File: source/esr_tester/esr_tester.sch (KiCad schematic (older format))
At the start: 40 parts, among them IC1-1 TL084, J1 Conn_01x01, J2 Conn_01x01

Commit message: Import netlist into Pcbnew.
Arrange footprints as in the magazine article.

Draw a board edge.
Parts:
- BT1: footprint Pin_Headers:Pin_Header_Straight_1x02_Pitch2.54mm -> Socket_Strips:Socket_Strip_Straight_1x01_Pitch2.54mm
- C3, C4: footprint Capacitors_THT:C_Disc_D3.0mm_W1.6mm_P2.50mm -> Capacitors_THT:C_Rect_L7.0mm_W2.5mm_P5.00mm
- C5, C6: footprint Capacitors_THT:C_Disc_D3.0mm_W1.6mm_P2.50mm -> Capacitors_THT:C_Rect_L7.0mm_W4.5mm_P5.00mm
- DS1, DS2, DS3: footprint Diodes_THT:D_5W_P5.08mm_Vertical_AnodeUp -> Diodes_THT:D_DO-35_SOD27_P7.62mm_Horizontal
- R1, R10, R11, R12, R13, R14, R15, R16, R17, R18, R19, R2, R20, R3, R4, R5, R6, R7, R8, R9: footprint Resistors_THT:R_Axial_DIN0204_L3.6mm_D1.6mm_P5.08mm_Horizontal -> Resistors_THT:R_Axial_DIN0204_L3.6mm_D1.6mm_P7.62mm_Horizontal
- R21: footprint Potentiometers:Potentiometer_Trimmer_ACP_CA9v_Horizontal_Px10.0mm_Py5.0mm -> Potentiometers:Potentiometer_Trimmer_Bourns_3266Y
- S1: footprint Buttons_Switches_THT:SW_PUSH-12mm -> Socket_Strips:Socket_Strip_Straight_1x03_Pitch2.54mm
- TR1, TR2, TR3: footprint TO_SOT_Packages_THT:TO-92_Molded_Narrow -> TO_SOT_Packages_THT:TO-92_Inline_Wide

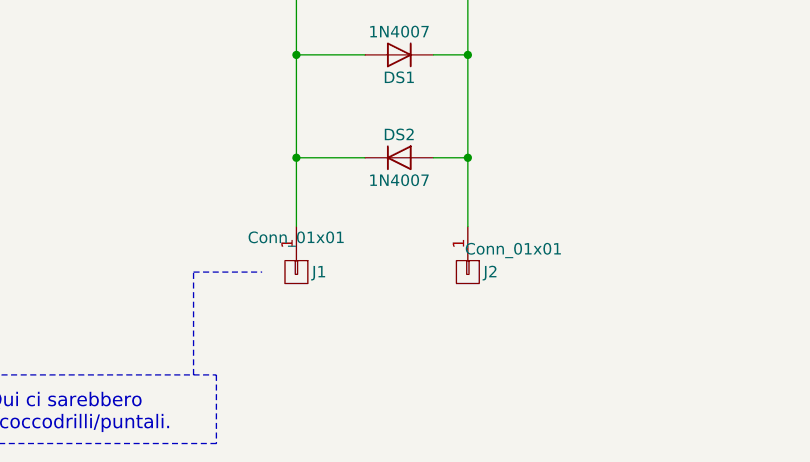
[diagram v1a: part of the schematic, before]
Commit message: The branch proto2 is for a prototype build with stripboard.
Schematics: changed connector for testing probes (one connector with
two poles instead of two with one each).

CvPcb: Changed some connectors, resistors and diodes footprints.

Pcbnew: A new layout for a stripboard.
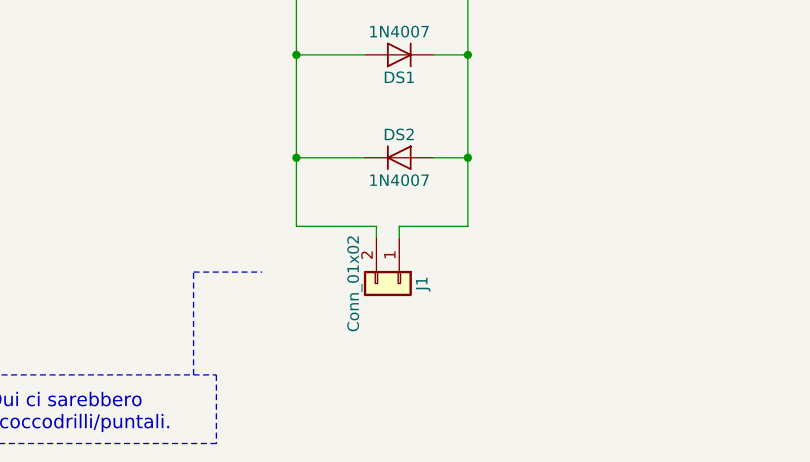
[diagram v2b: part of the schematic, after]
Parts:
- removed J1, J2: Conn_01x01, Connectors:Banana_Jack_1Pin, symbol CONN_01X01
- added J1: Conn_01x02, Socket_Strips:Socket_Strip_Straight_1x02_Pitch2.54mm, symbol Conn_01x02
- BT1: footprint Socket_Strips:Socket_Strip_Straight_1x01_Pitch2.54mm -> Socket_Strips:Socket_Strip_Straight_1x02_Pitch2.54mm
- DS1, DS2, DS3: footprint Diodes_THT:D_DO-35_SOD27_P7.62mm_Horizontal -> Diodes_THT:D_DO-35_SOD27_P2.54mm_Vertical_KathodeUp
- MES1: footprint Connectors:Banana_Jack_2Pin -> Socket_Strips:Socket_Strip_Straight_1x02_Pitch2.54mm
- R1, R10, R11, R12, R13, R14, R15, R16, R17, R18, R19, R2, R20, R3, R4, R5, R6, R7, R8, R9: footprint Resistors_THT:R_Axial_DIN0204_L3.6mm_D1.6mm_P7.62mm_Horizontal -> Resistors_THT:R_Axial_DIN0207_L6.3mm_D2.5mm_P2.54mm_Vertical
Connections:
- net GND: now also J1.1 (Pin_1)
- net at DS1.2 (A), DS2.1 (K), R10.2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: now also J1.2 (Pin_2)
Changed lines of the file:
@@
 F 0 "R4" V 2980 1300 50  0000 C CNN
 F 1 "10k" V 2900 1300 50  0000 C CNN
-F 2 "Resistors_THT:R_Axial_DIN0204_L3.6mm_D1.6mm_P7.62mm_Horizontal" V 2830 1300 50  0001 C CNN
+F 2 "Resistors_THT:R_Axial_DIN0207_L6.3mm_D2.5mm_P2.54mm_Vertical" V 2830 1300 50  0001 C CNN
 F 3 "" H 2900 1300 50  0001 C CNN
 	1    2900 1300
@@
 F 0 "R5" V 2980 2250 50  0000 C CNN
 F 1 "10k" V 2900 2250 50  0000 C CNN
-F 2 "Resistors_THT:R_Axial_DIN0204_L3.6mm_D1.6mm_P7.62mm_Horizontal" V 2830 2250 50  0001 C CNN
+F 2 "Resistors_THT:R_Axial_DIN0207_L6.3mm_D2.5mm_P2.54mm_Vertical" V 2830 2250 50  0001 C CNN
 F 3 "" H 2900 2250 50  0001 C CNN
 	1    2900 2250
@@
 F 0 "R1" V 1930 4600 50  0000 C CNN
 F 1 "1.5k" V 1850 4600 50  0000 C CNN
-F 2 "Resistors_THT:R_Axial_DIN0204_L3.6mm_D1.6mm_P7.62mm_Horizontal" V 1780 4600 50  0001 C CNN
+F 2 "Resistors_THT:R_Axial_DIN0207_L6.3mm_D2.5mm_P2.54mm_Vertical" V 1780 4600 50  0001 C CNN
 F 3 "" H 1850 4600 50  0001 C CNN
 	1    1850 4600
@@
 F 0 "R2" V 2730 3350 50  0000 C CNN
 F 1 "10k" V 2650 3350 50  0000 C CNN
-F 2 "Resistors_THT:R_Axial_DIN0204_L3.6mm_D1.6mm_P7.62mm_Horizontal" V 2580 3350 50  0001 C CNN
+F 2 "Resistors_THT:R_Axial_DIN0207_L6.3mm_D2.5mm_P2.54mm_Vertical" V 2580 3350 50  0001 C CNN
 F 3 "" H 2650 3350 50  0001 C CNN
 	1    2650 3350
@@
 F 0 "R3" V 2780 4600 50  0000 C CNN
 F 1 "10k" V 2700 4600 50  0000 C CNN
-F 2 "Resistors_THT:R_Axial_DIN0204_L3.6mm_D1.6mm_P7.62mm_Horizontal" V 2630 4600 50  0001 C CNN
+F 2 "Resistors_THT:R_Axial_DIN0207_L6.3mm_D2.5mm_P2.54mm_Vertical" V 2630 4600 50  0001 C CNN
 F 3 "" H 2700 4600 50  0001 C CNN
 	1    2700 4600
@@
 F 0 "R6" V 3280 3950 50  0000 C CNN
 F 1 "68k" V 3200 3950 50  0000 C CNN
-F 2 "Resistors_THT:R_Axial_DIN0204_L3.6mm_D1.6mm_P7.62mm_Horizontal" V 3130 3950 50  0001 C CNN
+F 2 "Resistors_THT:R_Axial_DIN0207_L6.3mm_D2.5mm_P2.54mm_Vertical" V 3130 3950 50  0001 C CNN
 F 3 "" H 3200 3950 50  0001 C CNN
 	1    3200 3950
@@
 F 0 "R8" V 3980 3300 50  0000 C CNN
 F 1 "12k" V 3900 3300 50  0000 C CNN
-F 2 "Resistors_THT:R_Axial_DIN0204_L3.6mm_D1.6mm_P7.62mm_Horizontal" V 3830 3300 50  0001 C CNN
+F 2 "Resistors_THT:R_Axial_DIN0207_L6.3mm_D2.5mm_P2.54mm_Vertical" V 3830 3300 50  0001 C CNN
 F 3 "" H 3900 3300 50  0001 C CNN
 	1    3900 3300
@@
 F 0 "R7" V 3980 1400 50  0000 C CNN
 F 1 "4.7k" V 3900 1400 50  0000 C CNN
-F 2 "Resistors_THT:R_Axial_DIN0204_L3.6mm_D1.6mm_P7.62mm_Horizontal" V 3830 1400 50  0001 C CNN
+F 2 "Resistors_THT:R_Axial_DIN0207_L6.3mm_D2.5mm_P2.54mm_Vertical" V 3830 1400 50  0001 C CNN
 F 3 "" H 3900 1400 50  0001 C CNN
 	1    3900 1400
@@
 F 0 "R9" V 4680 4500 50  0000 C CNN
 F 1 "1k" V 4600 4500 50  0000 C CNN
-F 2 "Resistors_THT:R_Axial_DIN0204_L3.6mm_D1.6mm_P7.62mm_Horizontal" V 4530 4500 50  0001 C CNN
+F 2 "Resistors_THT:R_Axial_DIN0207_L6.3mm_D2.5mm_P2.54mm_Vertical" V 4530 4500 50  0001 C CNN
 F 3 "" H 4600 4500 50  0001 C CNN
 F 4 "1%" V 4500 4500 60  0000 C CNN "Tolerance"
@@
 F 0 "R12" V 5180 4500 50  0000 C CNN
 F 1 "22R" V 5100 4500 50  0000 C CNN
-F 2 "Resistors_THT:R_Axial_DIN0204_L3.6mm_D1.6mm_P7.62mm_Horizontal" V 5030 4500 50  0001 C CNN
+F 2 "Resistors_THT:R_Axial_DIN0207_L6.3mm_D2.5mm_P2.54mm_Vertical" V 5030 4500 50  0001 C CNN
 F 3 "" H 5100 4500 50  0001 C CNN
 	1    5100 4500
@@
 F 0 "R10" V 4950 4750 50  0000 C CNN
 F 1 "22R" V 4850 4750 50  0000 C CNN
-F 2 "Resistors_THT:R_Axial_DIN0204_L3.6mm_D1.6mm_P7.62mm_Horizontal" V 4780 4750 50  0001 C CNN
+F 2 "Resistors_THT:R_Axial_DIN0207_L6.3mm_D2.5mm_P2.54mm_Vertical" V 4780 4750 50  0001 C CNN
 F 3 "" H 4850 4750 50  0001 C CNN
 	1    4850 4750
@@
 F 0 "R11" V 4930 4250 50  0000 C CNN
 F 1 "1k" V 4850 4250 50  0000 C CNN
-F 2 "Resistors_THT:R_Axial_DIN0204_L3.6mm_D1.6mm_P7.62mm_Horizontal" V 4780 4250 50  0001 C CNN
+F 2 "Resistors_THT:R_Axial_DIN0207_L6.3mm_D2.5mm_P2.54mm_Vertical" V 4780 4250 50  0001 C CNN
 F 3 "" H 4850 4250 50  0001 C CNN
 F 4 "1%" V 4750 4250 60  0000 C CNN "Tolerance"
@@
 F 0 "R13" V 5530 4050 50  0000 C CNN
 F 1 "1k" V 5450 4050 50  0000 C CNN
-F 2 "Resistors_THT:R_Axial_DIN0204_L3.6mm_D1.6mm_P7.62mm_Horizontal" V 5380 4050 50  0001 C CNN
+F 2 "Resistors_THT:R_Axial_DIN0207_L6.3mm_D2.5mm_P2.54mm_Vertical" V 5380 4050 50  0001 C CNN
 F 3 "" H 5450 4050 50  0001 C CNN
 	1    5450 4050
@@
 F 0 "R14" V 5530 4250 50  0000 C CNN
 F 1 "1k" V 5450 4250 50  0000 C CNN
-F 2 "Resistors_THT:R_Axial_DIN0204_L3.6mm_D1.6mm_P7.62mm_Horizontal" V 5380 4250 50  0001 C CNN
+F 2 "Resistors_THT:R_Axial_DIN0207_L6.3mm_D2.5mm_P2.54mm_Vertical" V 5380 4250 50  0001 C CNN
 F 3 "" H 5450 4250 50  0001 C CNN
 	1    5450 4250
@@
 F 0 "R16" V 5980 4550 50  0000 C CNN
 F 1 "47k" V 5900 4550 50  0000 C CNN
-F 2 "Resistors_THT:R_Axial_DIN0204_L3.6mm_D1.6mm_P7.62mm_Horizontal" V 5830 4550 50  0001 C CNN
+F 2 "Resistors_THT:R_Axial_DIN0207_L6.3mm_D2.5mm_P2.54mm_Vertical" V 5830 4550 50  0001 C CNN
 F 3 "" H 5900 4550 50  0001 C CNN
 	1    5900 4550
@@
 F 0 "R15" V 5980 3750 50  0000 C CNN
 F 1 "47k" V 5900 3750 50  0000 C CNN
-F 2 "Resistors_THT:R_Axial_DIN0204_L3.6mm_D1.6mm_P7.62mm_Horizontal" V 5830 3750 50  0001 C CNN
+F 2 "Resistors_THT:R_Axial_DIN0207_L6.3mm_D2.5mm_P2.54mm_Vertical" V 5830 3750 50  0001 C CNN
 F 3 "" H 5900 3750 50  0001 C CNN
 	1    5900 3750
@@
 F 0 "R18" V 7180 4150 50  0000 C CNN
 F 1 "15k" V 7100 4150 50  0000 C CNN
-F 2 "Resistors_THT:R_Axial_DIN0204_L3.6mm_D1.6mm_P7.62mm_Horizontal" V 7030 4150 50  0001 C CNN
+F 2 "Resistors_THT:R_Axial_DIN0207_L6.3mm_D2.5mm_P2.54mm_Vertical" V 7030 4150 50  0001 C CNN
 F 3 "" H 7100 4150 50  0001 C CNN
 	1    7100 4150
@@
 F 0 "R19" V 8180 3150 50  0000 C CNN
 F 1 "680R" V 8100 3150 50  0000 C CNN
-F 2 "Resistors_THT:R_Axial_DIN0204_L3.6mm_D1.6mm_P7.62mm_Horizontal" V 8030 3150 50  0001 C CNN
+F 2 "Resistors_THT:R_Axial_DIN0207_L6.3mm_D2.5mm_P2.54mm_Vertical" V 8030 3150 50  0001 C CNN
 F 3 "" H 8100 3150 50  0001 C CNN
 	1    8100 3150
@@
 F 0 "R17" V 6380 2550 50  0000 C CNN
 F 1 "47k" V 6300 2550 50  0000 C CNN
-F 2 "Resistors_THT:R_Axial_DIN0204_L3.6mm_D1.6mm_P7.62mm_Horizontal" V 6230 2550 50  0001 C CNN
+F 2 "Resistors_THT:R_Axial_DIN0207_L6.3mm_D2.5mm_P2.54mm_Vertical" V 6230 2550 50  0001 C CNN
 F 3 "" H 6300 2550 50  0001 C CNN
 	1    6300 2550
@@
 F 0 "DS3" H 7250 2200 50  0000 C CNN
 F 1 "1N4148" H 7250 2000 50  0000 C CNN
-F 2 "Diodes_THT:D_DO-35_SOD27_P7.62mm_Horizontal" H 7250 2100 50  0001 C CNN
+F 2 "Diodes_THT:D_DO-35_SOD27_P2.54mm_Vertical_KathodeUp" H 7250 2100 50  0001 C CNN
 F 3 "" H 7250 2100 50  0001 C CNN
 	1    7250 2100
@@
 F 0 "R20" V 8530 2100 50  0000 C CNN
 F 1 "2.2k" V 8450 2100 50  0000 C CNN
-F 2 "Resistors_THT:R_Axial_DIN0204_L3.6mm_D1.6mm_P7.62mm_Horizontal" V 8380 2100 50  0001 C CNN
+F 2 "Resistors_THT:R_Axial_DIN0207_L6.3mm_D2.5mm_P2.54mm_Vertical" V 8380 2100 50  0001 C CNN
 F 3 "" H 8450 2100 50  0001 C CNN
 	1    8450 2100
@@
 F 0 "MES1" H 8670 3140 50  0000 R CNN
 F 1 "Amperemeter_DC" H 9500 2900 50  0001 R CNN
-F 2 "Connectors:Banana_Jack_2Pin" V 8800 3200 50  0001 C CNN
+F 2 "Socket_Strips:Socket_Strip_Straight_1x02_Pitch2.54mm" V 8800 3200 50  0001 C CNN
 F 3 "" V 8800 3200 50  0001 C CNN
 	1    8800 3100
@@
 F 0 "DS1" H 4800 5450 50  0000 C CNN
 F 1 "1N4007" H 4800 5250 50  0000 C CNN
-F 2 "Diodes_THT:D_DO-35_SOD27_P7.62mm_Horizontal" H 4800 5350 50  0001 C CNN
+F 2 "Diodes_THT:D_DO-35_SOD27_P2.54mm_Vertical_KathodeUp" H 4800 5350 50  0001 C CNN
 F 3 "" H 4800 5350 50  0001 C CNN
 	1    4800 5350
@@
 F 0 "DS2" H 4800 5900 50  0000 C CNN
 F 1 "1N4007" H 4800 5700 50  0000 C CNN
-F 2 "Diodes_THT:D_DO-35_SOD27_P7.62mm_Horizontal" H 4800 5800 50  0001 C CNN
+F 2 "Diodes_THT:D_DO-35_SOD27_P2.54mm_Vertical_KathodeUp" H 4800 5800 50  0001 C CNN
 F 3 "" H 4800 5800 50  0001 C CNN
 	1    4800 5800
 	1    0    0    -1
-$EndComp
-$Comp
-L CONN_01X01 J1
-U 1 1 59E325E9
-P 4350 6300
-F 0 "J1" V 4350 6400 50  0000 C CNN
-F 1 "Conn_01x01" V 4200 6300 50  0000 C CNN
-F 2 "Connectors:Banana_Jack_1Pin" H 4350 6300 50  0001 C CNN
-F 3 "" H 4350 6300 50  0001 C CNN
-	1    4350 6300
-	0    1    1    0
-$EndComp
-$Comp
-L CONN_01X01 J2
-U 1 1 59E326D8
-P 5100 6300
-F 0 "J2" V 5100 6400 50  0000 C CNN
-F 1 "Conn_01x01" V 5000 6500 50  0000 C CNN
-F 2 "Connectors:Banana_Jack_1Pin" H 5100 6300 50  0001 C CNN
-F 3 "" H 5100 6300 50  0001 C CNN
-	1    5100 6300
-	0    1    1    0
 $EndComp
 $Bitmap
@@
 F 0 "BT1" H 950 2300 50  0000 L CNN
 F 1 "9V" H 950 2200 50  0000 L CNN
-F 2 "Socket_Strips:Socket_Strip_Straight_1x01_Pitch2.54mm" V 850 2260 50  0001 C CNN
+F 2 "Socket_Strips:Socket_Strip_Straight_1x02_Pitch2.54mm" V 850 2260 50  0001 C CNN
 F 3 "" V 850 2260 50  0001 C CNN
 	1    850  2200
@@
 	4350 5800 4650 5800
 Wire Wire Line
-	4350 4750 4350 6100
-Wire Wire Line
 	4650 5350 4350 5350
 Connection ~ 4350 5800
@@
 Text Notes 9450 2650 0    60   ~ 0
 Add a Power Flag to \nindicate to KiCad that \npower comes from somewhere. \nThis will avoid the ERC warning.
+$Comp
+L Conn_01x02 J1
+U 1 1 5A2EA64A
+P 4800 6350
+F 0 "J1" H 4800 6450 50  0000 C CNN
+F 1 "Conn_01x02" H 4800 6150 50  0000 C CNN
+F 2 "Socket_Strips:Socket_Strip_Straight_1x02_Pitch2.54mm" H 4800 6350 50  0001 C CNN
+F 3 "" H 4800 6350 50  0001 C CNN
+	1    4800 6350
+	0    1    1    0
+$EndComp
+Wire Wire Line
+	4350 4750 4350 6100
+Wire Wire Line
+	5100 6100 4800 6100
+Wire Wire Line
+	4800 6100 4800 6150
+Wire Wire Line
+	4350 6100 4700 6100
+Wire Wire Line
+	4700 6100 4700 6150
 $EndSCHEMATC
